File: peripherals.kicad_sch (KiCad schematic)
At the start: 6 parts, among them Q1 BSS138, SW2 SW_ACK, U6 TSOP384xx

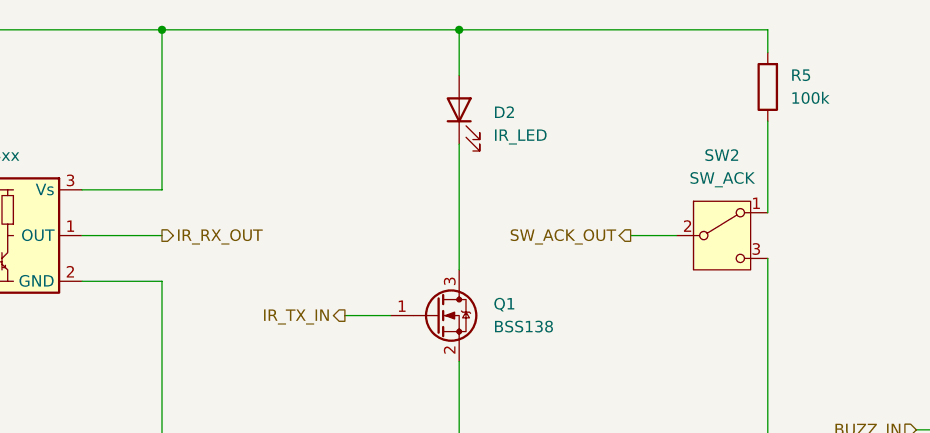
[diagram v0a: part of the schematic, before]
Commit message: Place ~18–22 Ω (for ~100 mA pulsed) in series with D2.
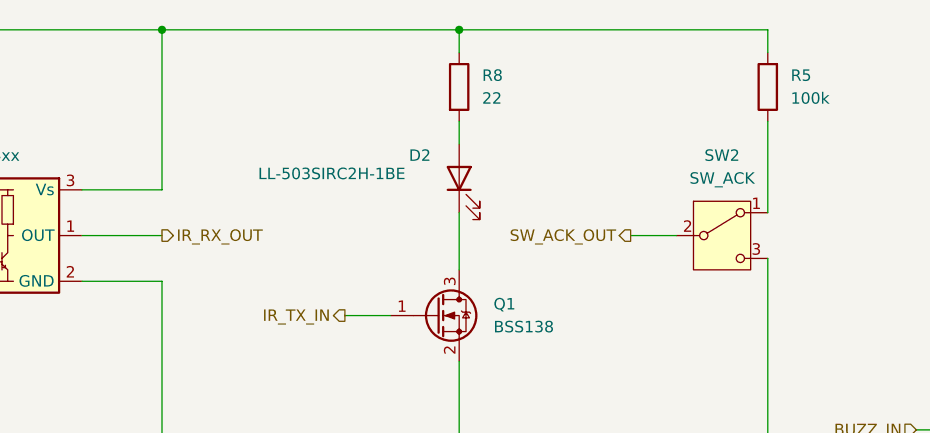
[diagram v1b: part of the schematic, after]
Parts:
- added R8: 22, symbol Device:R
- D2: value IR_LED -> LL-503SIRC2H-1BE
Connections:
- net 3.3V: now also R8.1; no longer D2.2 (A)
- new net: D2.2 (A), R8.2
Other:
- moved on the sheet: D2
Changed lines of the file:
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@@
+	(wire
+		(pts
+			(xy 114.3 58.42) (xy 114.3 64.77)
+		)
+		(stroke
+			(width 0)
+			(type default)
+		)
+	)
 	(wire
 		(pts
@@
 	(wire
 		(pts
-			(xy 148.59 38.1) (xy 114.3 38.1)
-		)
-		(stroke
-			(width 0)
-			(type default)
-		)
-	)
-	(wire
-		(pts
 			(xy 72.39 60.96) (xy 81.28 60.96)
 		)
@@
 	(wire
 		(pts
-			(xy 114.3 38.1) (xy 81.28 38.1)
+			(xy 81.28 38.1) (xy 114.3 38.1)
 		)
 		(stroke
@@
 	(wire
 		(pts
+			(xy 114.3 38.1) (xy 148.59 38.1)
+		)
+		(stroke
+			(width 0)
+			(type default)
+		)
+	)
+	(wire
+		(pts
 			(xy 81.28 87.63) (xy 114.3 87.63)
 		)
@@
 	(wire
 		(pts
-			(xy 114.3 43.18) (xy 114.3 38.1)
-		)
-		(stroke
-			(width 0)
-			(type default)
-		)
-	)
-	(wire
-		(pts
 			(xy 81.28 38.1) (xy 43.18 38.1)
 		)
@@
 	(wire
 		(pts
+			(xy 114.3 48.26) (xy 114.3 50.8)
+		)
+		(stroke
+			(width 0)
+			(type default)
+		)
+	)
+	(wire
+		(pts
+			(xy 114.3 38.1) (xy 114.3 40.64)
+		)
+		(stroke
+			(width 0)
+			(type default)
+		)
+	)
+	(wire
+		(pts
 			(xy 81.28 87.63) (xy 43.18 87.63)
 		)
@@
 		(pts
 			(xy 72.39 55.88) (xy 81.28 55.88)
-		)
-		(stroke
-			(width 0)
-			(type default)
-		)
-	)
-	(wire
-		(pts
-			(xy 114.3 50.8) (xy 114.3 64.77)
 		)
 		(stroke
@@
 	(symbol
 		(lib_id "Device:LED")
-		(at 114.3 46.99 90)
+		(at 114.3 54.61 90)
 		(unit 1)
 		(exclude_from_sim no)
@@
 		(on_board yes)
 		(dnp no)
-		(fields_autoplaced yes)
 		(property "Reference" "D2"
-			(at 118.11 47.3074 90)
+			(at 108.712 52.07 90)
 			(effects
 				(font
@@
 			)
 		)
-		(property "Value" "IR_LED"
-			(at 118.11 49.8474 90)
+		(property "Value" "LL-503SIRC2H-1BE"
+			(at 91.948 54.102 90)
 			(effects
 				(font
@@
 		)
 		(property "Footprint" ""
-			(at 114.3 46.99 0)
+			(at 114.3 54.61 0)
 			(effects
 				(font
@@
 		)
 		(property "Datasheet" "~"
-			(at 114.3 46.99 0)
+			(at 114.3 54.61 0)
 			(effects
 				(font
@@
 		)
 		(property "Description" "Light emitting diode"
-			(at 114.3 46.99 0)
+			(at 114.3 54.61 0)
 			(effects
 				(font
@@
 		)
 		(property "Sim.Pins" "1=K 2=A"
-			(at 114.3 46.99 0)
+			(at 114.3 54.61 0)
 			(effects
 				(font
@@
 					(unit 1)
 				)
+			)
+		)
+	)
+	(symbol
+		(lib_id "Device:R")
+		(at 114.3 44.45 0)
+		(unit 1)
+		(exclude_from_sim no)
+		(in_bom yes)
+		(on_board yes)
+		(dnp no)
+		(fields_autoplaced yes)
+		(property "Reference" "R8"
+			(at 116.84 43.1799 0)
+			(effects
+				(font
+					(size 1.27 1.27)
+				)
+				(justify left)
+			)
+		)
+		(property "Value" "22"
+			(at 116.84 45.7199 0)
+			(effects
+				(font
+					(size 1.27 1.27)
+				)
+				(justify left)
+			)
+		)
+		(property "Footprint" ""
+			(at 112.522 44.45 90)
+			(effects
+				(font
+					(size 1.27 1.27)
+				)
+				(hide yes)
+			)
+		)
+		(property "Datasheet" "~"
+			(at 114.3 44.45 0)
+			(effects
+				(font
+					(size 1.27 1.27)
+				)
+				(hide yes)
+			)
+		)
+		(property "Description" "Resistor"
+			(at 114.3 44.45 0)
+			(effects
+				(font
+					(size 1.27 1.27)
+				)
+				(hide yes)
+			)
+		)
+		(pin "2"
+		)
+		(pin "1"
+		)
+		(instances
+			(project ""
+				(path "/64404f27-cfd6-41d9-8edb-810ebab8cc14/ed770b04-6f81-410b-b0ec-7aa50308ff69"
+					(reference "R8")
+					(unit 1)
+				)

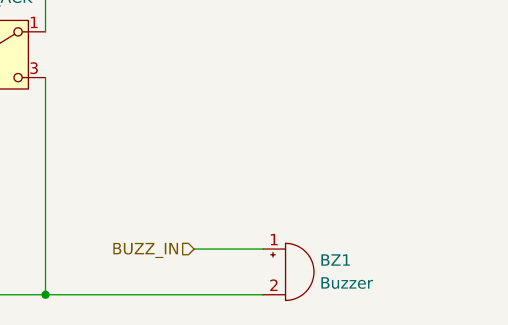
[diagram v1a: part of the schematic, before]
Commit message: Use LPT1440S-HS-05 as the buzzer.
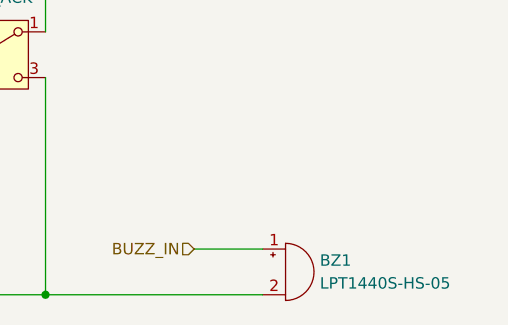
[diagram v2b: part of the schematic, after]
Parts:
- BZ1: value Buzzer -> LPT1440S-HS-05
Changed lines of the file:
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@@
 			)
 		)
-		(property "Value" "Buzzer"
+		(property "Value" "LPT1440S-HS-05"
 			(at 179.07 86.3599 0)
 			(effects

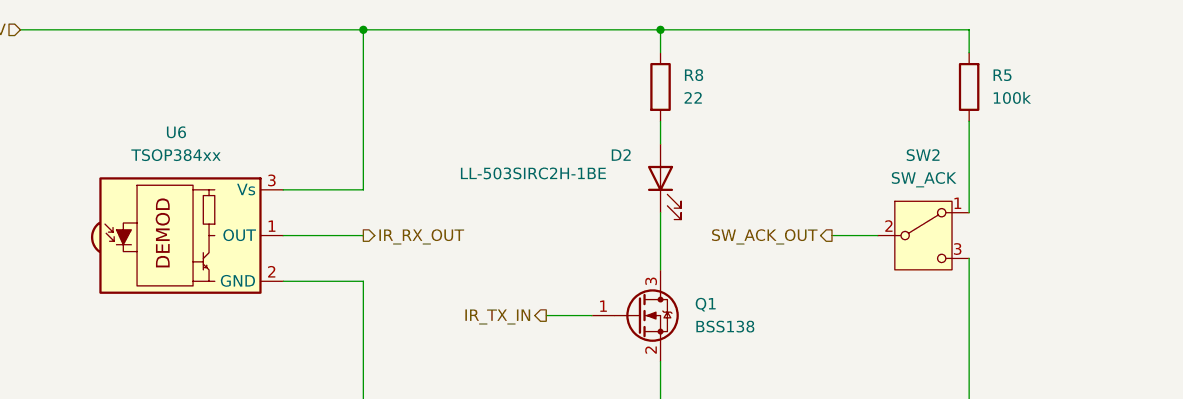
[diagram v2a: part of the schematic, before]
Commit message: Re-labelled all parts.
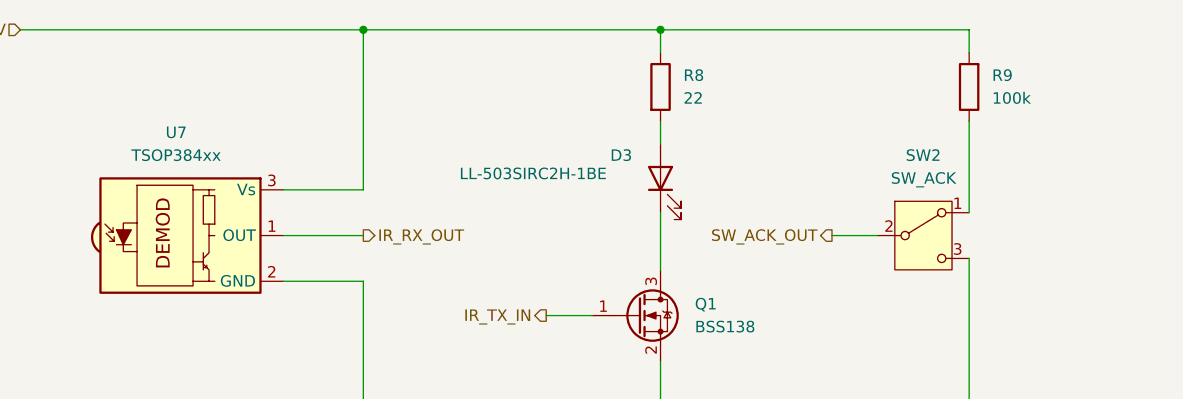
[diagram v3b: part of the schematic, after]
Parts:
- renumbered D2 to D3, R5 to R9, U6 to U7
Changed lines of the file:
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@@
 		(on_board yes)
 		(dnp no)
-		(property "Reference" "D2"
+		(property "Reference" "D3"
 			(at 108.712 52.07 90)
 			(effects
@@
 			(project "universal-board"
 				(path "/64404f27-cfd6-41d9-8edb-810ebab8cc14/ed770b04-6f81-410b-b0ec-7aa50308ff69"
-					(reference "D2")
+					(reference "D3")
 					(unit 1)
 				)
@@
 		(dnp no)
 		(fields_autoplaced yes)
-		(property "Reference" "R5"
+		(property "Reference" "R9"
 			(at 151.13 43.1799 0)
 			(effects
@@
 			(project "universal-board"
 				(path "/64404f27-cfd6-41d9-8edb-810ebab8cc14/ed770b04-6f81-410b-b0ec-7aa50308ff69"
-					(reference "R5")
+					(reference "R9")
 					(unit 1)
 				)
@@
 		(dnp no)
 		(fields_autoplaced yes)
-		(property "Reference" "U6"
+		(property "Reference" "U7"
 			(at 60.495 49.53 0)
 			(effects
@@
 			(project "universal-board"
 				(path "/64404f27-cfd6-41d9-8edb-810ebab8cc14/ed770b04-6f81-410b-b0ec-7aa50308ff69"
-					(reference "U6")
-					(unit 1)
-				)
+					(reference "U7")
+					(unit 1)
+				)

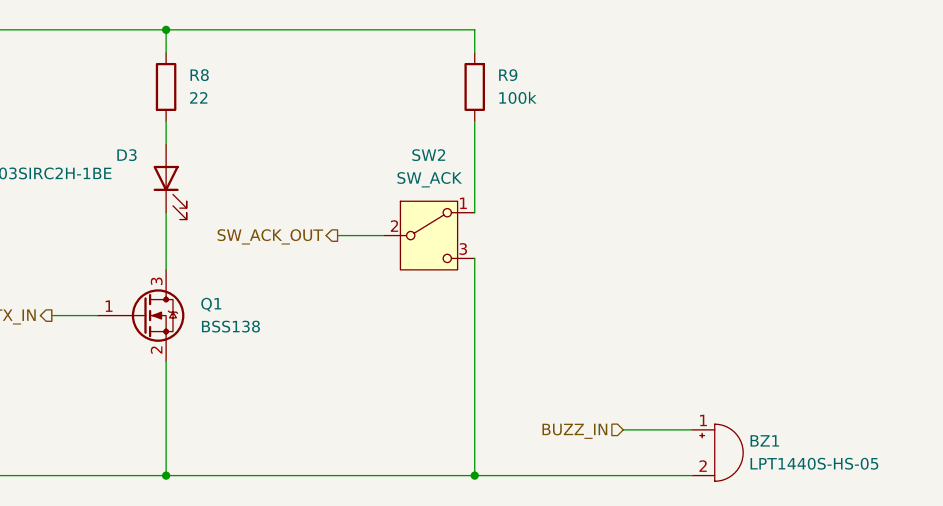
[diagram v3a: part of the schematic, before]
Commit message: - added bidirectional TVS between VBUS & GND - USB-C shield and GND are now connected - added comments re pin order - removed pull-up resistor on SW_ACK_INPUT because it's configured as INPUT_PULLUP
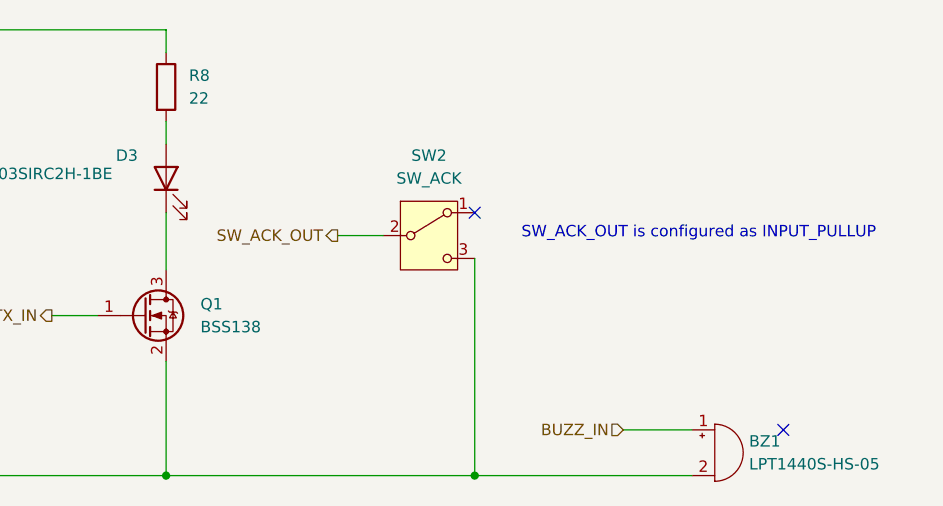
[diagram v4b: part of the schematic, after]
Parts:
- removed R9: 100k, symbol Device:R
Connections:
- no-connect marks 0 -> 2
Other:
- note added: "SW_ACK_OUT is configured as INPUT_PULLUP"
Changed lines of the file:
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@@
 	(generator_version "9.0")
 	(paper "A4")
-	(junction
-		(at 114.3 38.1)
-		(diameter 0)
-		(color 0 0 0 0)
+	(text "SW_ACK_OUT is configured as INPUT_PULLUP"
+		(exclude_from_sim no)
+		(at 173.482 60.706 0)
+		(effects
+			(font
+				(size 1.27 1.27)
+			)
+		)
 	)
 	(junction
@@
 		(color 0 0 0 0)
 	)
+	(no_connect
+		(at 148.59 58.42)
+	)
+	(no_connect
+		(at 182.88 82.55)
+	)
 	(wire
 		(pts
@@
 	(wire
 		(pts
-			(xy 148.59 40.64) (xy 148.59 38.1)
-		)
-		(stroke
-			(width 0)
-			(type default)
-		)
-	)
-	(wire
-		(pts
 			(xy 114.3 58.42) (xy 114.3 64.77)
 		)
@@
 	(wire
 		(pts
-			(xy 114.3 38.1) (xy 148.59 38.1)
-		)
-		(stroke
-			(width 0)
-			(type default)
-		)
-	)
-	(wire
-		(pts
 			(xy 81.28 87.63) (xy 114.3 87.63)
 		)
@@
 		(pts
 			(xy 81.28 38.1) (xy 43.18 38.1)
-		)
-		(stroke
-			(width 0)
-			(type default)
-		)
-	)
-	(wire
-		(pts
-			(xy 148.59 48.26) (xy 148.59 58.42)
 		)
 		(stroke
@@
 					(unit 1)
 				)
-			)
-		)
-	)
-	(symbol
-		(lib_id "Device:R")
-		(at 148.59 44.45 180)
-		(unit 1)
-		(exclude_from_sim no)
-		(in_bom yes)
-		(on_board yes)
-		(dnp no)
-		(fields_autoplaced yes)
-		(property "Reference" "R9"
-			(at 151.13 43.1799 0)
-			(effects
-				(font
-					(size 1.27 1.27)
-				)
-				(justify right)
-			)
-		)
-		(property "Value" "100k"
-			(at 151.13 45.7199 0)
-			(effects
-				(font
-					(size 1.27 1.27)
-				)
-				(justify right)
-			)
-		)
-		(property "Footprint" ""
-			(at 150.368 44.45 90)
-			(effects
-				(font
-					(size 1.27 1.27)
-				)
-				(hide yes)
-			)
-		)
-		(property "Datasheet" "~"
-			(at 148.59 44.45 0)
-			(effects
-				(font
-					(size 1.27 1.27)
-				)
-				(hide yes)
-			)
-		)
-		(property "Description" "Resistor"
-			(at 148.59 44.45 0)
-			(effects
-				(font
-					(size 1.27 1.27)
-				)
-				(hide yes)
-			)
-		)
-		(pin "1"
-		)
-		(pin "2"
-		)
-		(instances
-			(project "universal-board"
-				(path "/64404f27-cfd6-41d9-8edb-810ebab8cc14/ed770b04-6f81-410b-b0ec-7aa50308ff69"
-					(reference "R9")
-					(unit 1)
-				)
